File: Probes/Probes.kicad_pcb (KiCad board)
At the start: 2 copper layers, 73.2 x 39 mm, 44 parts, among them IC1 ADUM1251ARZ, J1 Conn_Coaxial, J2 Conn_01x02_Male, J3 Conn_01x05_Male, J4 Conn_01x05_Male, U1 LMC6042IN, U3 ADS1014IDGS

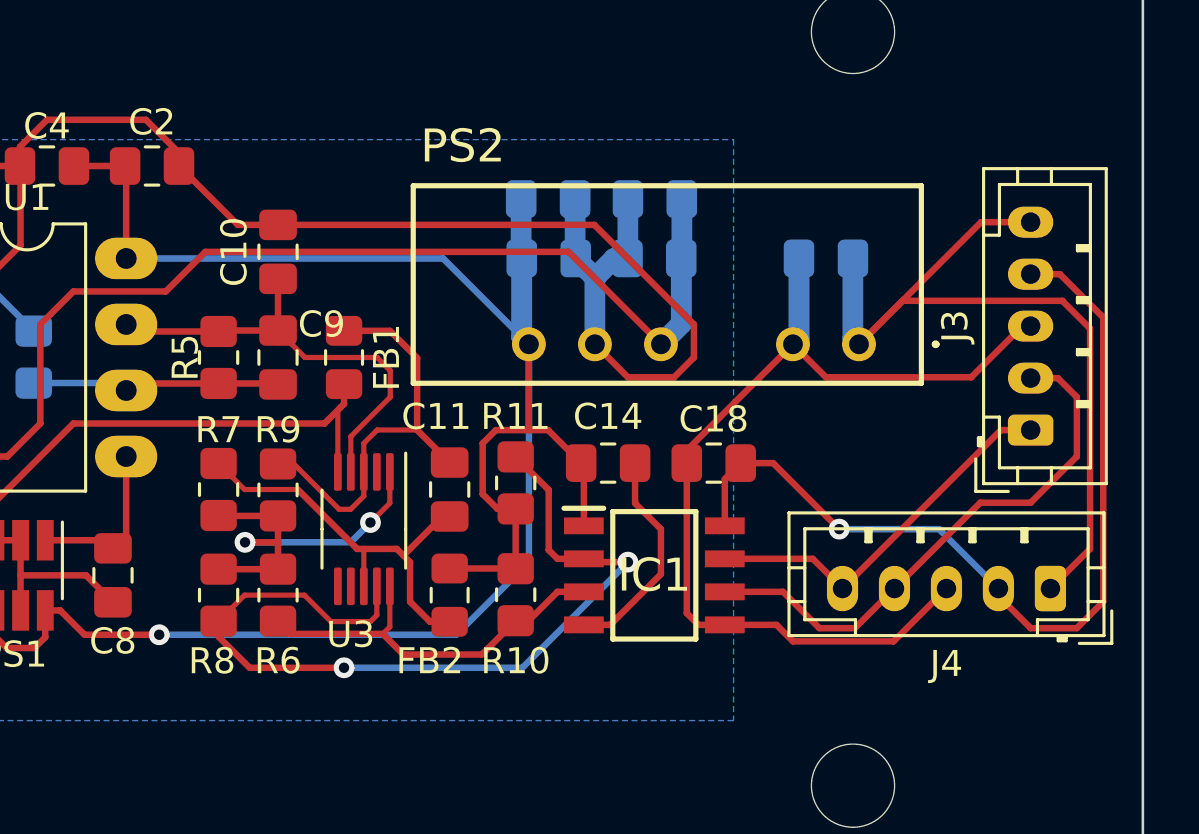
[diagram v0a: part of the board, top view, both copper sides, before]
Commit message: invert ADUM1251 invert J3
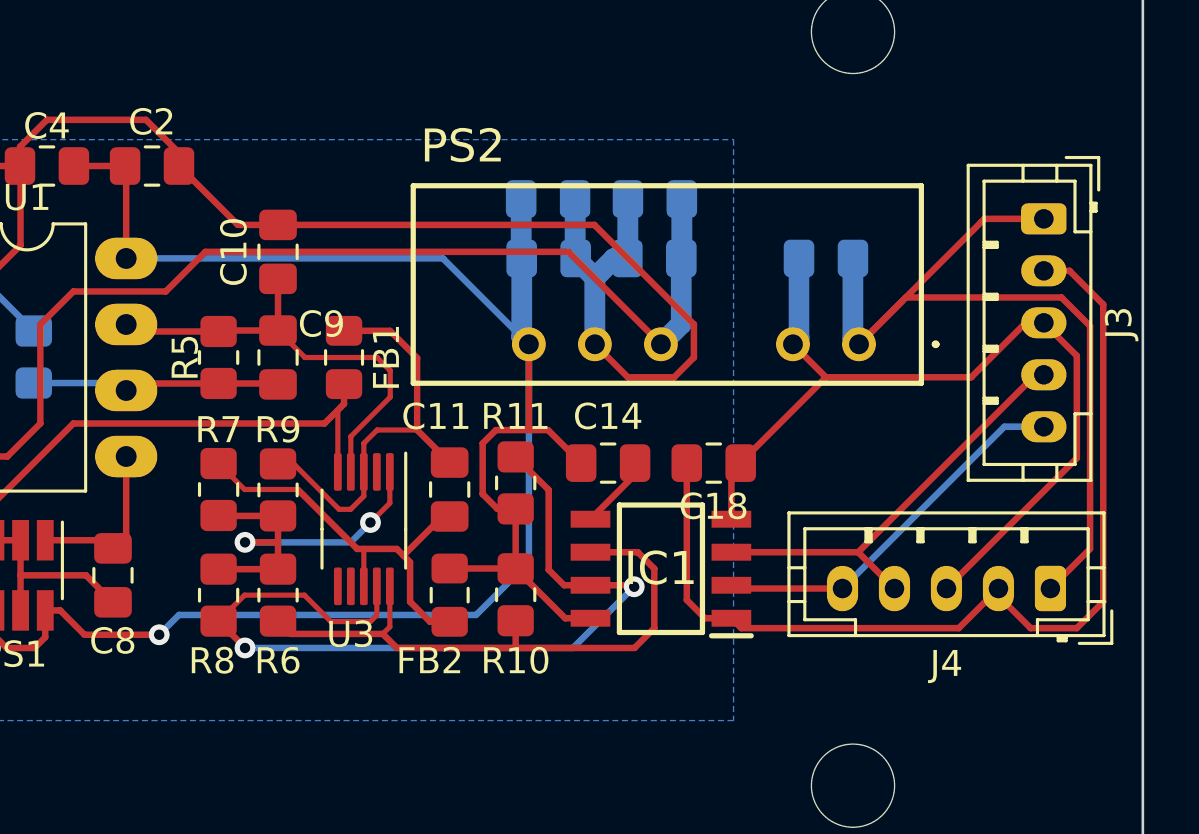
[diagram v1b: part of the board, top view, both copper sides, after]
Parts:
- moved J3 8.14 mm to (133.6, 74.2), turned to 270 degrees
- moved IC1 0.36 mm to (118.9, 87.6), turned to 180 degrees
- turned C18 to 180 degrees
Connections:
- IC1 pad 1: +5V -> +3.3VP
- IC1 pad 2: Net-(IC1-Pad2) -> SDA
- IC1 pad 3: Net-(IC1-Pad3) -> SCL
- IC1 pad 4: Net-(C14-Pad1) -> GNDPWR
- IC1 pad 5: GNDPWR -> Net-(C14-Pad1)
- IC1 pad 6: SCL -> Net-(IC1-Pad6)
- IC1 pad 7: SDA -> Net-(IC1-Pad7)
- IC1 pad 8: +3.3VP -> +5V
- J3 pad 1: SDA -> +5VP
- J3 pad 2: SCL -> +3.3VP
- J3 pad 4: +3.3VP -> SCL
- J3 pad 5: +5VP -> SDA
- R10 pad 2: Net-(IC1-Pad3) -> Net-(IC1-Pad6)
- R11 pad 2: Net-(IC1-Pad2) -> Net-(IC1-Pad7)
- R6 pad 1: Net-(IC1-Pad3) -> Net-(IC1-Pad6)
- R8 pad 1: Net-(IC1-Pad2) -> Net-(IC1-Pad7)
- U3 pad 10: Net-(IC1-Pad3) -> Net-(IC1-Pad6)
- U3 pad 9: Net-(IC1-Pad2) -> Net-(IC1-Pad7)
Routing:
- net Net-(IC1-Pad2): track 34.0 -> 0.00 mm, vias 2 -> 0
- net Net-(IC1-Pad7): track 0.00 -> 34.0 mm, vias 0 -> 2
- net Net-(IC1-Pad6): track 0.00 -> 23.7 mm
- net Net-(IC1-Pad3): track 15.2 -> 0.00 mm
- net Net-(C14-Pad1): track 8.46 -> 2.87 mm
- net SCL: track 21.2 -> 16.8 mm
- net +3.3VP: track 34.3 -> 38.3 mm, vias 1 -> 0
- net GNDPWR: track 37.2 -> 34.2 mm
- net +5V: track 81.9 -> 83.2 mm
- net +5VP: track 32.6 -> 33.2 mm

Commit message: missing gnd missing pull up resistor on DC/DC
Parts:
- added J5: Conn_01x01_Female, Connector_PinSocket_2.00mm:PinSocket_1x01_P2.00mm_Vertical, F.Cu at (83.6, 89.2)
- added J6: Conn_01x01_Female, Connector_PinSocket_2.00mm:PinSocket_1x01_P2.00mm_Vertical, F.Cu at (104.1, 71.4)
- added J7: Conn_01x01_Female, Connector_PinSocket_2.00mm:PinSocket_1x01_P2.00mm_Vertical, F.Cu at (102.9, 93.7)
- added J8: Conn_01x01_Female, Connector_PinSocket_2.00mm:PinSocket_1x01_P2.00mm_Vertical, F.Cu at (113.3, 93.5)
- added R12: 2700, Resistor_SMD:R_0805_2012Metric_Pad1.20x1.40mm_HandSolder, B.Cu at (129.8, 80.3)
- added R13: 2700, Resistor_SMD:R_0805_2012Metric_Pad1.20x1.40mm_HandSolder, B.Cu at (125.7, 84.6)
- added R14: 560, Resistor_SMD:R_0805_2012Metric_Pad1.20x1.40mm_HandSolder, B.Cu at (114.6, 70.9)
- added R15: 560, Resistor_SMD:R_0805_2012Metric_Pad1.20x1.40mm_HandSolder, B.Cu at (118.6, 70.9)
- C10, C5: value 100nF -> DNP
- C3: value 1uF -> 47nF DNP
- R10, R11: value 200 -> 2700
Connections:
- C1 pad 2: Net-(C1-Pad2) -> GND
- C14 pad 1: Net-(C14-Pad1) -> GND
- C8 pad 2: Net-(C1-Pad2) -> GND
- IC1 pad 5: Net-(C14-Pad1) -> GND
- PS1 pad 2: Net-(C1-Pad2) -> GND
- PS1 pad 3: Net-(C1-Pad2) -> GND
- PS1 pad 5: Net-(C1-Pad2) -> GND
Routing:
- net GND: track 108.2 -> 134.8 mm
- net Net-(C10-Pad1): track 17.9 -> 32.2 mm
- net +3.3VP: track 38.3 -> 50.3 mm
- net Net-(C1-Pad2): track 9.76 -> 0.00 mm
- net Net-(IC1-Pad6): track 23.7 -> 27.6 mm
- net Net-(IC1-Pad7): track 34.0 -> 37.0 mm
- net Net-(C14-Pad1): track 2.87 -> 0.00 mm
- net SCL: track 16.8 -> 19.7 mm
- net SDA: track 14.7 -> 17.5 mm
- net -5V: track 47.4 -> 50.0 mm
- net +5V: track 83.2 -> 85.8 mm

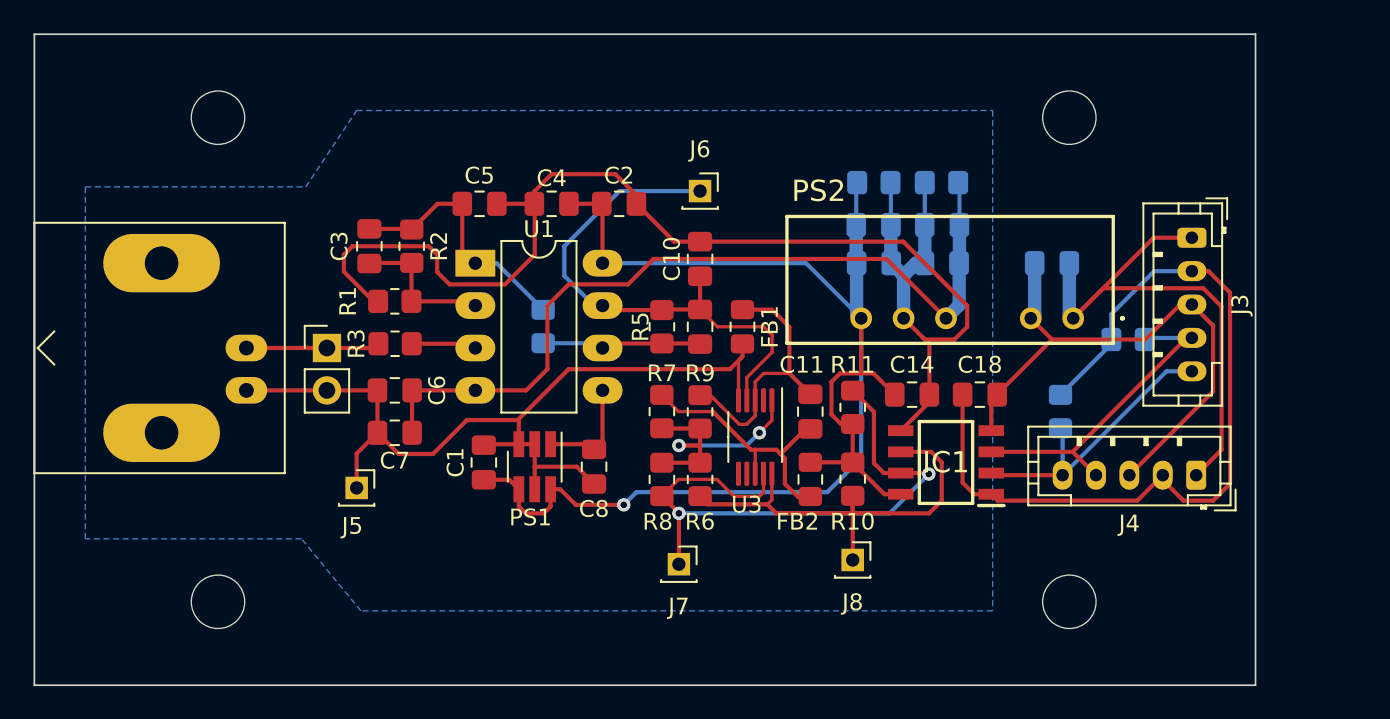
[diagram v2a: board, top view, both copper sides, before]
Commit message: move mounting hole
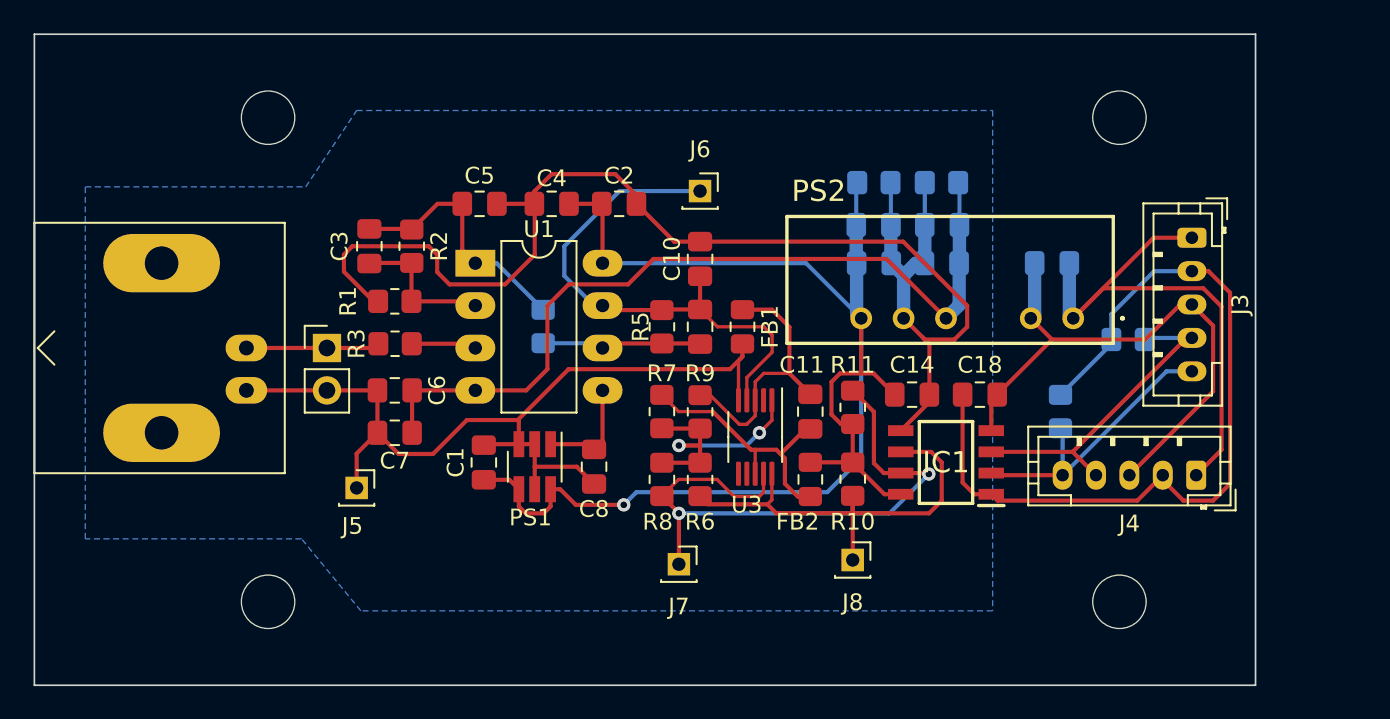
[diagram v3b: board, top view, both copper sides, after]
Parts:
- moved REF** 3.00 mm to (129.3, 67.0)
- moved REF** 3.00 mm to (129.3, 96.0)
- moved REF** 3.00 mm to (78.3, 96.0)
- moved REF** 3.00 mm to (78.3, 67.0)

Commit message: horizontal connector
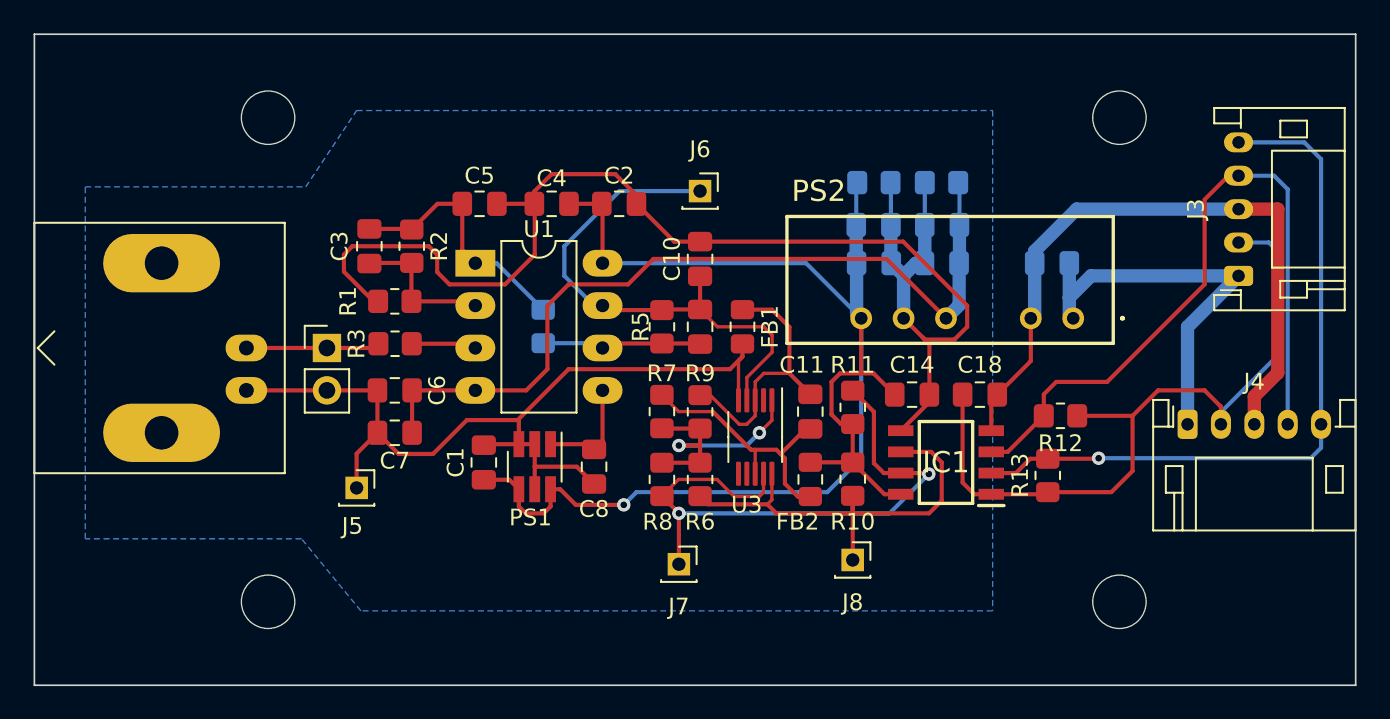
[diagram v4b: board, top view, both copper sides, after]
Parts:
- J3, J4: footprint Connector_JST:JST_PH_B5B-PH-K_1x05_P2.00mm_Vertical -> Connector_JST:JST_PH_S5B-PH-K_1x05_P2.00mm_Horizontal
- R12, R13: moved to F.Cu
- moved R12 6.11 mm to (125.7, 84.8), turned to 180 degrees
- moved R13 3.90 mm to (125.0, 88.4), turned to 90 degrees
- moved J3 3.61 mm to (136.4, 76.5), turned to 90 degrees
- moved J4 3.09 mm to (133.3, 85.3), turned to 0 degrees
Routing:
- net SDA: track 17.5 -> 43.2 mm, vias 0 -> 1
- net SCL: track 19.7 -> 42.8 mm
- net +5VP: track 33.2 -> 24.2 mm
- net GNDPWR: track 34.2 -> 40.9 mm
- net +3.3VP: track 50.3 -> 45.1 mm
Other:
- board size 73.2 x 39 mm -> 79.2 x 39 mm
